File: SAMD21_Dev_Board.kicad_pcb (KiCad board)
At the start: 2 copper layers, 55.4 x 87.4 mm, 89 parts, among them J1 SWD, J10 JST_SH_SM06B-SRSS-TB_1x06-1MP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, J11 JST_SH_SM06B-SRSS-TB_1x06-1MP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, J12 JST_SH_SM06B-SRSS-TB_1x06-1MP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, J13 JST_SH_SM06B-SRSS-TB_1x06-1MP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, J14 JST_SH_SM06B-SRSS-TB_1x06-1MP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, J15 JST_SH_SM06B-SRSS-TB_1x06-1MP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, J16 JST_SH_SM06B-SRSS-TB_1x06-1MP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, J17 Status LED, J18 Screw_Terminal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

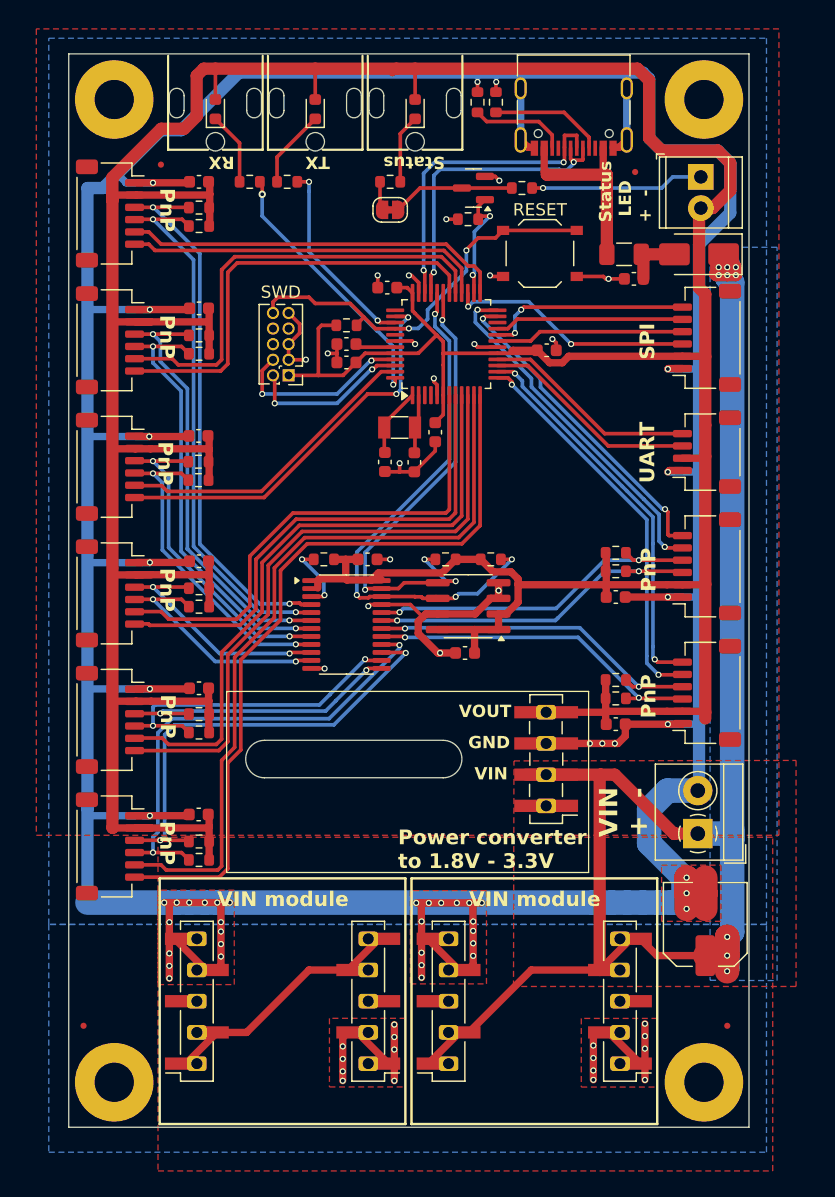
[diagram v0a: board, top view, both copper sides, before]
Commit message: SWD port moved closer to the edge to be able use the pogo pins clip
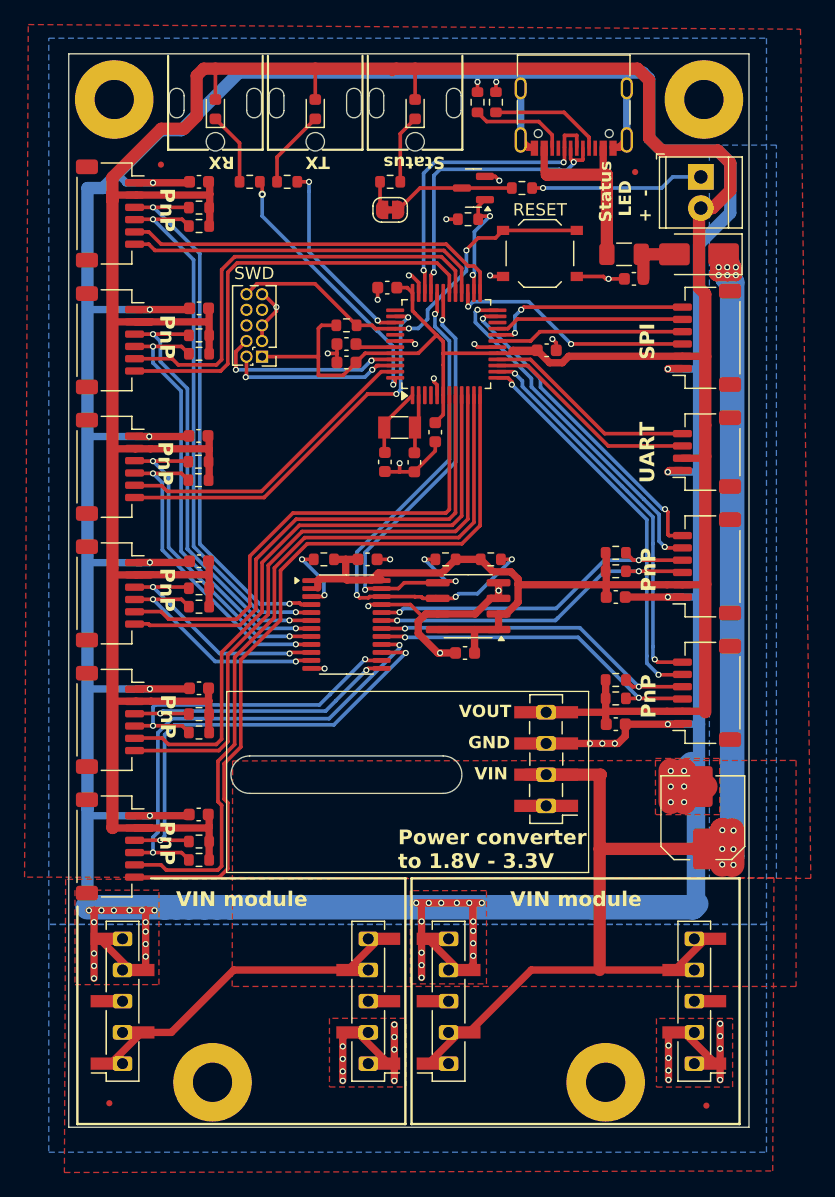
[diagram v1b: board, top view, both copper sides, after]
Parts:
- removed J18: Screw_Terminal, TerminalBlock_4Ucon:TerminalBlock_4Ucon_1x02_P3.50mm_Horizontal
- moved C11 8.69 mm to (133.9, 112.0)
- moved REF** 8.00 mm to (94.0, 133.5)
- moved REF** 8.00 mm to (126.0, 133.5)
- moved REF** 6.72 mm to (134.2, 135.4)
- moved REF** 6.64 mm to (85.6, 135.2)
- moved J6 6.05 mm to (133.2, 126.9)
- moved J20 6.05 mm to (86.7, 126.9)
- moved J1 2.64 mm to (98.0, 74.4)
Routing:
- net GND: track 466.8 -> 474.0 mm, vias 80 -> 83
- net VDC: track 156.9 -> 154.7 mm, vias 9 -> 12
- net VCC: track 374.2 -> 375.8 mm
- net SWCLK: track 15.1 -> 16.1 mm
- net SWDIO: track 13.4 -> 14.4 mm
- net RESET: track 32.7 -> 33.6 mm
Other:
- outline, holes or cut-outs redrawn
- board text removed: "VIN + -"

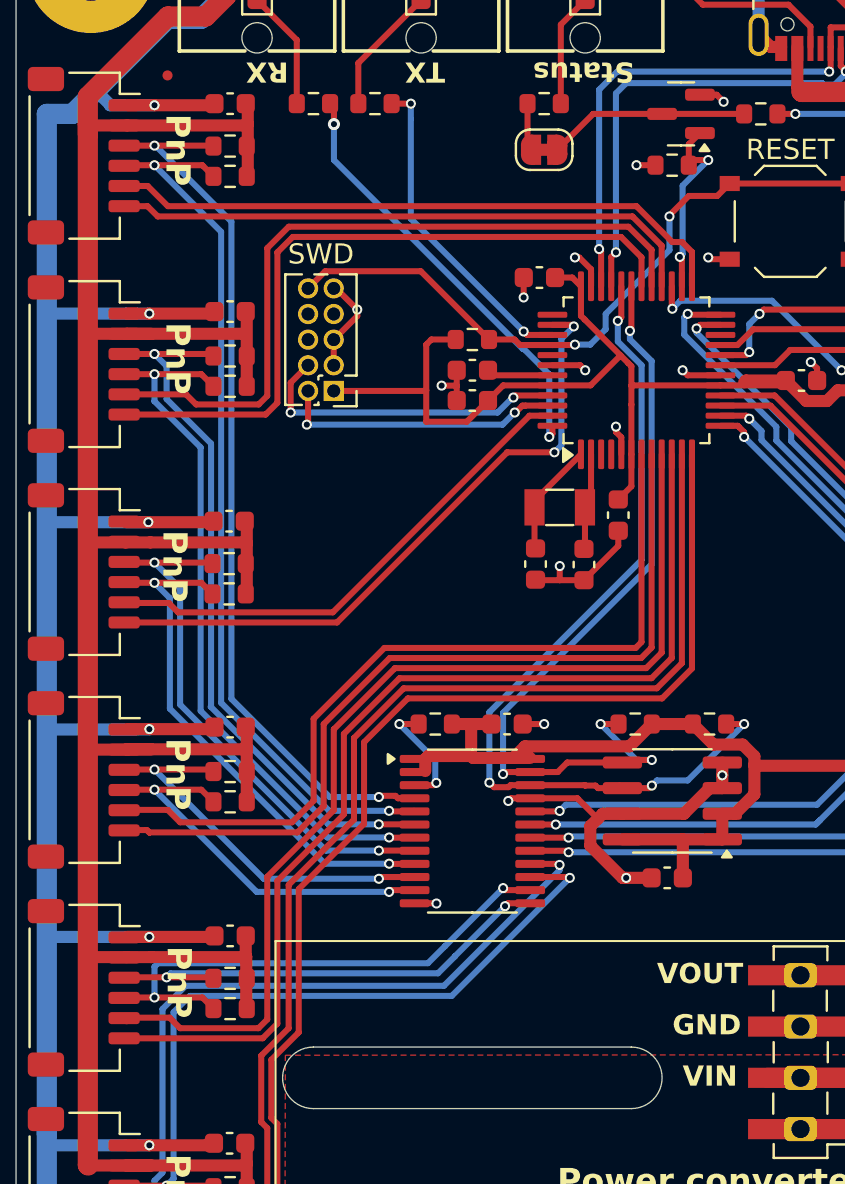
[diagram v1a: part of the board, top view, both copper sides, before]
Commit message: Minor cosmetic trace routing changes
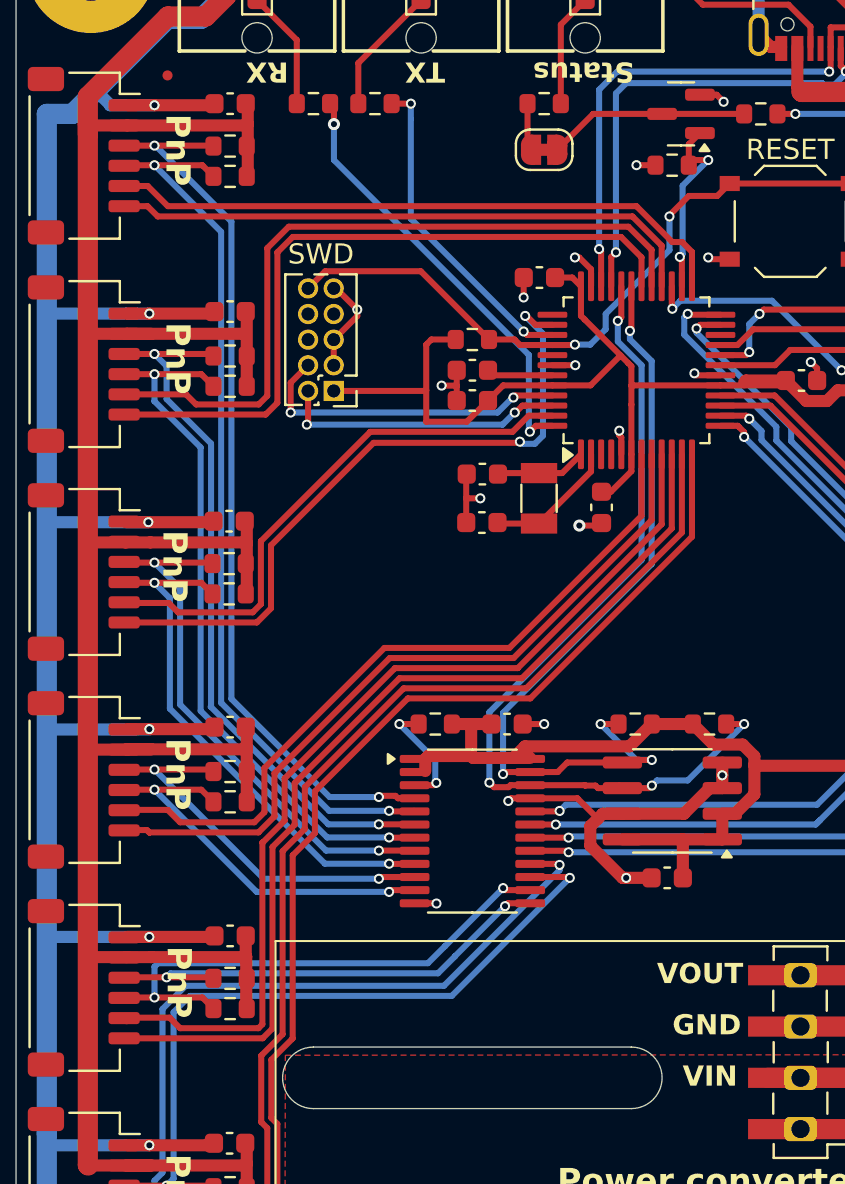
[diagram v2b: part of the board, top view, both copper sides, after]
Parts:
- moved C13 5.47 mm to (105.4, 81.0), turned to 0 degrees
- moved C12 5.18 mm to (105.4, 78.5), turned to 0 degrees
- moved Y1 1.12 mm to (108.2, 79.8), turned to 90 degrees
- moved C17 0.91 mm to (111.3, 80.2)
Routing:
- net A2: track 41.8 -> 37.0 mm
- net A1: track 41.2 -> 36.4 mm
- net D9: track 62.5 -> 58.6 mm
- net D8: track 61.7 -> 57.9 mm
- net A4: track 51.5 -> 47.7 mm
- net A3: track 50.8 -> 47.1 mm
- net GND: track 474.0 -> 470.5 mm, vias 83 -> 84
- net Net-(U3-PA01): track 5.19 -> 7.35 mm
- net D31: track 32.6 -> 34.5 mm
- net A5: track 25.3 -> 27.2 mm
- net Net-(U3-PA00): track 5.66 -> 4.87 mm

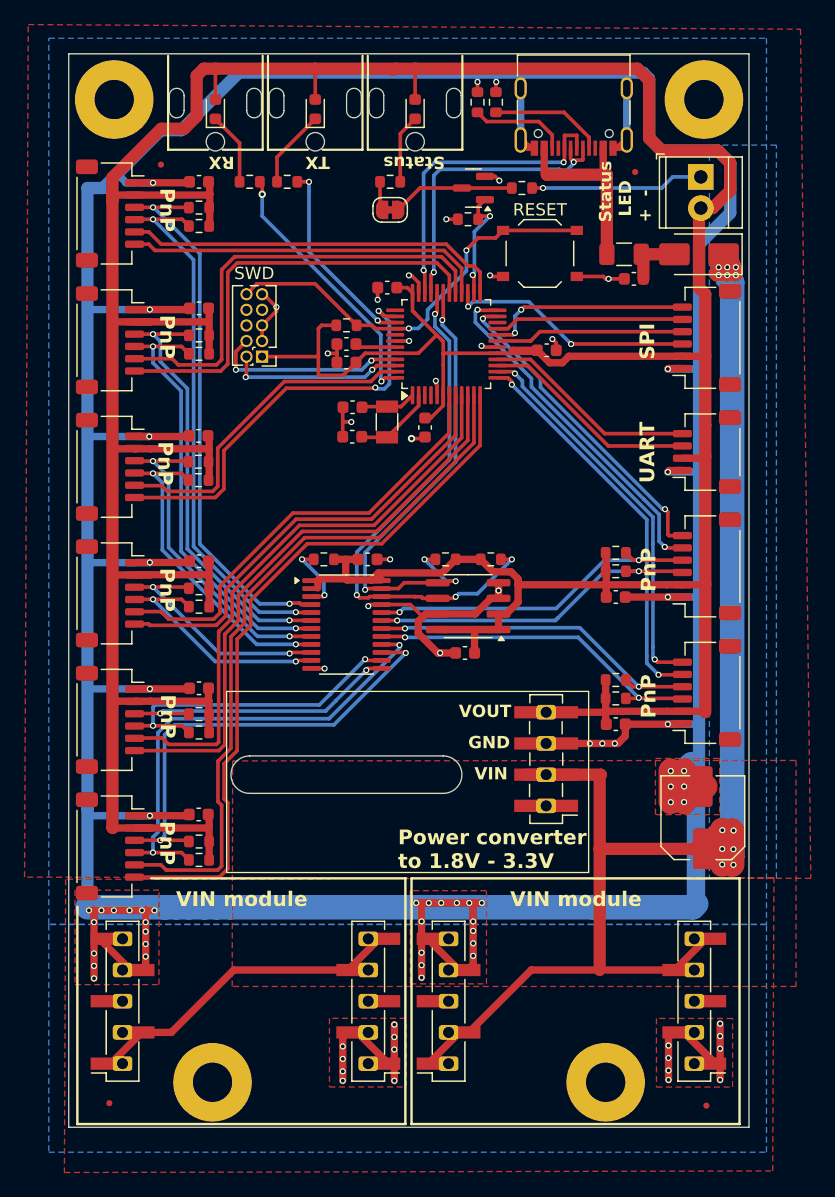
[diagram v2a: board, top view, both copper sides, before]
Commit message: Fiducials change to 1mm footprint Using D4 line for status LED (can do PWM) instead of D13 Bootloader updated accordingly
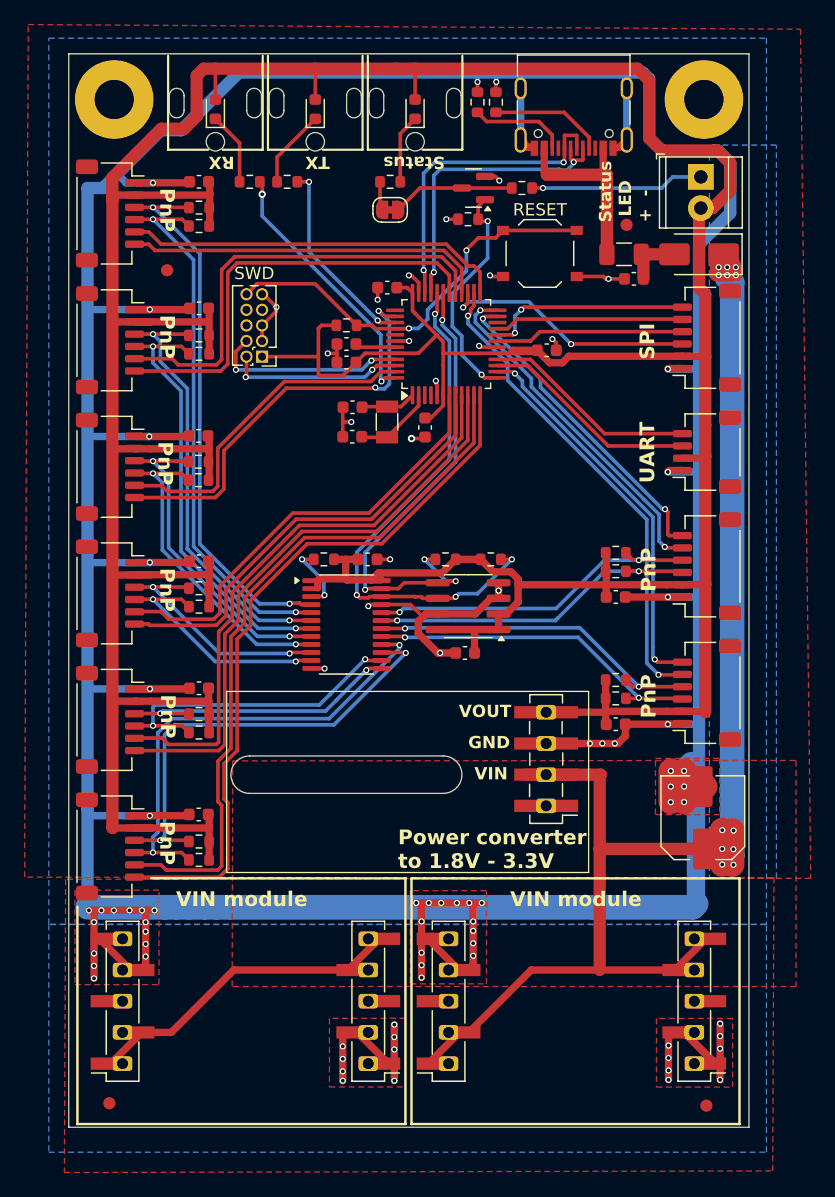
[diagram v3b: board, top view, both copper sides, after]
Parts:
- removed the REF** at (94.0, 133.5)
- removed the REF** at (126.0, 133.5)
- F1: value 500mA -> 2.2A
- REF** (x4): value Fiducial_0.5mm_Mask1mm -> Fiducial_1mm_Mask2mm; footprint Fiducial:Fiducial_0.5mm_Mask1mm -> Fiducial:Fiducial_1mm_Mask2mm
- moved REF** 8.61 mm to (90.3, 67.4)
- moved REF** 4.36 mm to (127.7, 63.7)
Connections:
- J10 pad 5: D4 -> D13
- Q1 pad 1: D13 -> D4
- R21 pad 1: D13 -> D4
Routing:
- net D13: track 9.76 -> 39.7 mm
- net D4: track 32.1 -> 19.1 mm
- net D10/SPI_SS: track 20.2 -> 20.8 mm

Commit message: Power modules are set wider, to have more space for XT30 connectors. Interrupt lines were changed based on the SAMD21 interrupt mapping. PnP connector lines were swapped to match colors on the JST-SH-06 cables available from Pololu. Status LED line changed to be one of the lines that are left, that have PWM capability.
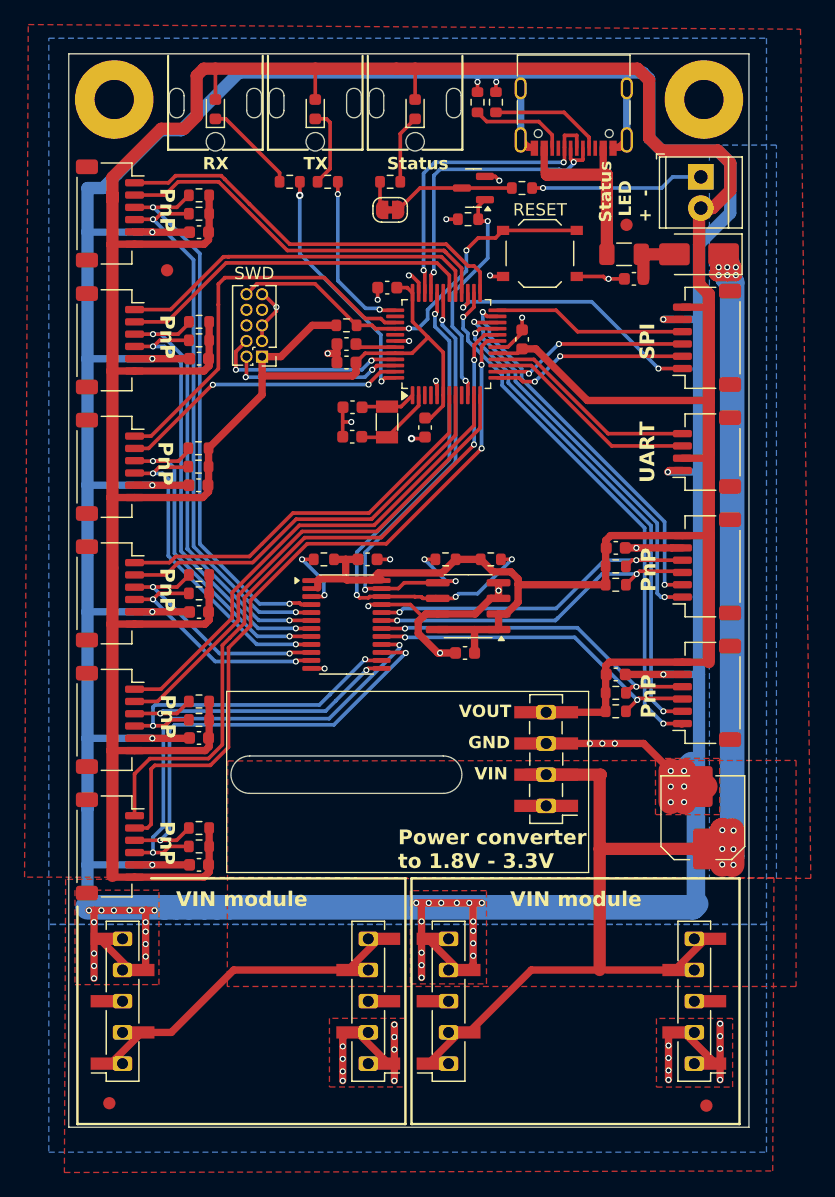
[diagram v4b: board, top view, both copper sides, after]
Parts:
- moved G*** 66.1 mm to (95.0, 125.8)
- moved C9 4.13 mm to (92.9, 95.2)
- moved C8 4.10 mm to (92.9, 115.8)
- moved C5 4.10 mm to (92.9, 74.6)
- moved C4 4.10 mm to (92.9, 64.3)
- moved C6 4.05 mm to (126.8, 100.3)
- moved C10 4.04 mm to (92.9, 105.5)
- moved C7 4.02 mm to (92.9, 84.9)
- moved C3 4.00 mm to (126.8, 90.0)
- moved R24 3.30 mm to (103.4, 60.2)
- moved R25 3.26 mm to (100.3, 60.2)
- moved C18 2.19 mm to (119.2, 73.0), turned to -90 degrees
- moved R14 1.10 mm to (92.9, 114.3)
- moved R15 1.10 mm to (92.9, 112.8)
- moved R8 1.10 mm to (92.9, 73.1)
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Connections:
- J10 pad 1: GND -> D13
- J10 pad 2: VCC -> D22
- J10 pad 5: D13 -> GND
- J10 pad 6: D3 -> VCC
- J11 pad 1: GND -> D24
- J11 pad 2: VCC -> D23
- J11 pad 5: D8 -> GND
- J11 pad 6: D9 -> VCC
- J12 pad 1: GND -> D8
- J12 pad 2: VCC -> D9
- J12 pad 5: A3 -> GND
- J12 pad 6: A4 -> VCC
- J13 pad 1: GND -> D11
- J13 pad 2: VCC -> D12
- J13 pad 5: D11 -> GND
- J13 pad 6: D12 -> VCC
- J14 pad 1: GND -> D6
- J14 pad 2: VCC -> D7
- J14 pad 5: D6 -> GND
- J14 pad 6: D7 -> VCC
- J15 pad 1: GND -> D26
- J15 pad 2: VCC -> A5
- J15 pad 5: A5 -> GND
- J15 pad 6: D31 -> VCC
- J16 pad 1: GND -> A1
- J16 pad 2: VCC -> A2
- J16 pad 5: A1 -> GND
- J16 pad 6: A2 -> VCC
- J8 pad 1: GND -> D10/SPI_SS
- J8 pad 2: VCC -> SPI_MOSI
- J8 pad 3: D10/SPI_SS -> SPI_MISO
- J8 pad 4: SPI_MOSI -> SPI_SCK
- J8 pad 5: SPI_MISO -> GND
- J8 pad 6: SPI_SCK -> VCC
- J9 pad 1: GND -> D38
- J9 pad 2: VCC -> D2
- J9 pad 5: D5 -> GND
- J9 pad 6: D2 -> VCC
- Q1 pad 1: D4 -> A4
- R21 pad 1: D4 -> A4
- U3 pad 13: D4 -> SPI_MOSI
- U3 pad 14: D3 -> SPI_MISO
- U3 pad 19: SPI_MOSI -> D23
- U3 pad 20: SPI_SCK -> D24
- U3 pad 21: SPI_MISO -> D22
- U3 pad 24: D5 -> SPI_SCK
- U3 pad 37: D30 -> TX_LED
- U3 pad 39: TX_LED -> D26
- U3 pad 41: unconnected-(U3-PA28-Pad41) -> D27/USB_HOST
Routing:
- net D23: track 0.00 -> 59.4 mm, vias 0 -> 2
- net D24: track 0.00 -> 58.4 mm, vias 0 -> 2
- net A3: track 47.1 -> 0.00 mm
- net D22: track 0.00 -> 40.6 mm, vias 0 -> 2
- net D31: track 34.5 -> 0.00 mm, vias 2 -> 0
- net D38: track 0.00 -> 32.4 mm, vias 0 -> 2
- net D26: track 0.00 -> 32.1 mm
- net D3: track 31.8 -> 0.00 mm, vias 2 -> 0
- net A4: track 47.7 -> 18.9 mm, vias 0 -> 2
- net D5: track 28.8 -> 0.00 mm, vias 2 -> 0
- net D4: track 19.1 -> 0.00 mm, vias 2 -> 0
- net D8: track 57.9 -> 40.2 mm
- net D9: track 58.6 -> 41.2 mm
- net GND: track 470.7 -> 481.9 mm, vias 84 -> 83
- net D6: track 36.4 -> 30.2 mm
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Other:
- board text added: "INT2 INT1 SDA SCL GND VCC"
- board text added: "PnP #0"
- board text added: "Rx Tx VCC GND"
- board text added: "VCC GND SCK MISO MOSI SS"

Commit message: Kikit panelization
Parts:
- moved JP1 0.52 mm to (108.5, 63.0)
- moved R23 0.50 mm to (108.5, 60.7)
- moved R24 0.50 mm to (103.4, 60.7)
- moved R25 0.50 mm to (100.3, 60.7)
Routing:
- net RX_LED: track 20.3 -> 19.7 mm
- net TX_LED: track 13.7 -> 13.2 mm
- net Net-(D2-K): track 5.62 -> 6.12 mm
- net Net-(D4-K): track 7.78 -> 8.28 mm
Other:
- board text added: "Power converter to 2.0V - 3.3V"
- board text added: "Status LED - +"
- board text removed: "PnP #0"
- board text removed: "Power converter to 1.8V - 3.3V"
